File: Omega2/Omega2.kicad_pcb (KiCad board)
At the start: 2 copper layers, 6 parts, among them J1 Conn_01x04_Female, J2 Conn_01x14_Female, SW1 SW_DIP_x01, U1 Omega2+

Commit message: Organización display, botón de reset, power flag
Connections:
- net +3V3 renamed 3.3V
- net Net-(R1-Pad2) renamed Om38
- net Net-(U1-Pad11) renamed Om8
- net Net-(U1-Pad12) renamed Om7
- net Net-(U1-Pad13) renamed Om6
- net Net-(U1-Pad7) renamed Om15
- U1 pad 10: unconnected-(U1-Pad10) -> Om9
- U1 pad 14: unconnected-(U1-Pad14) -> Om1
- U1 pad 15: unconnected-(U1-Pad15) -> Om0
- U1 pad 16: unconnected-(U1-Pad16) -> OmRSTneg
- U1 pad 17: unconnected-(U1-Pad17) -> Om5
- U1 pad 18: unconnected-(U1-Pad18) -> Om4
- U1 pad 19: unconnected-(U1-Pad19) -> Om19
- U1 pad 2: unconnected-(U1-Pad2) -> Om11
- U1 pad 20: unconnected-(U1-Pad20) -> Om18
- U1 pad 21: unconnected-(U1-Pad21) -> OmRx+
- U1 pad 22: unconnected-(U1-Pad22) -> OmRx-
- U1 pad 23: unconnected-(U1-Pad23) -> OmTx+
- U1 pad 24: unconnected-(U1-Pad24) -> OmTx-
- U1 pad 25: unconnected-(U1-Pad25) -> Om3.3V
- U1 pad 27: unconnected-(U1-Pad27) -> Om12
- U1 pad 28: unconnected-(U1-Pad28) -> Om13
- U1 pad 29: unconnected-(U1-Pad29) -> OmUSB-
- U1 pad 3: unconnected-(U1-Pad3) -> Om3
- U1 pad 30: unconnected-(U1-Pad30) -> OmUSB+
- U1 pad 4: unconnected-(U1-Pad4) -> Om2
- U1 pad 5: unconnected-(U1-Pad5) -> Om17
- U1 pad 6: unconnected-(U1-Pad6) -> Om16
- U1 pad 8: unconnected-(U1-Pad8) -> Om46
- U1 pad 9: unconnected-(U1-Pad9) -> Om45

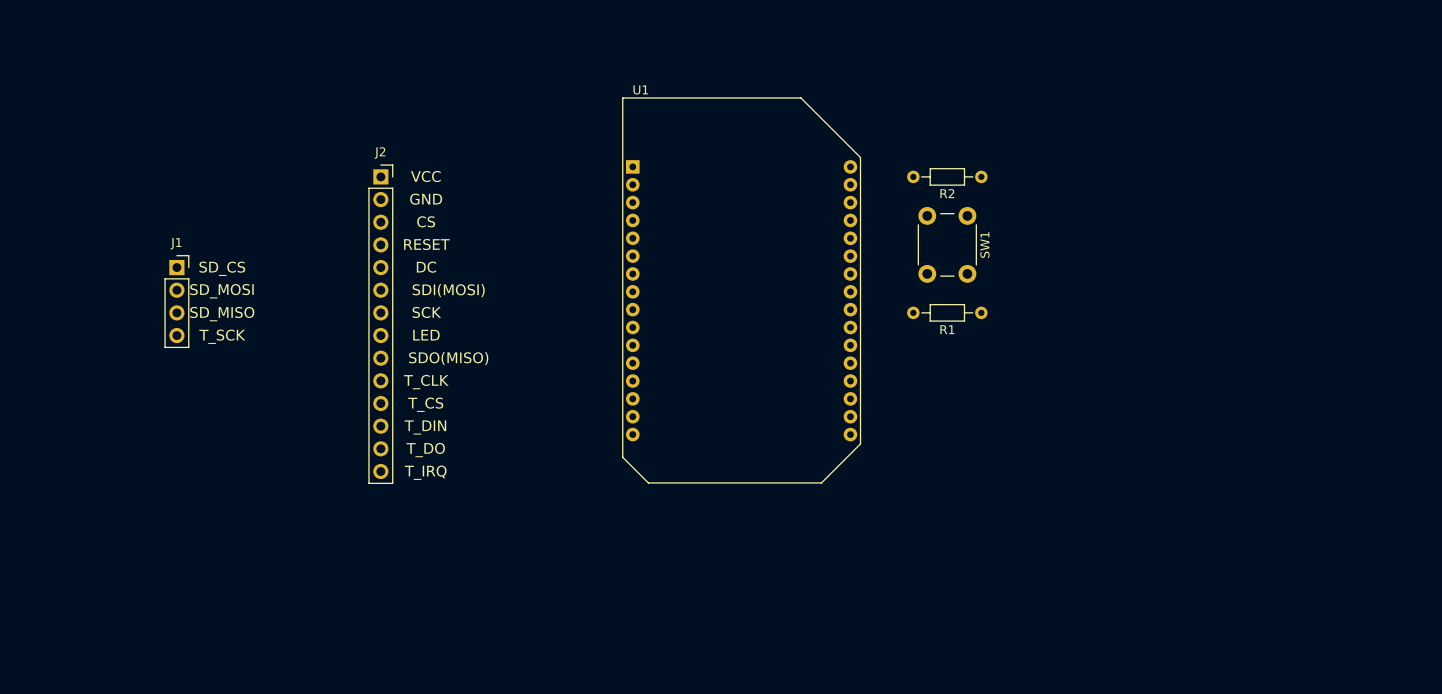
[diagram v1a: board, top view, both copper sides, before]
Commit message: edicion pcb
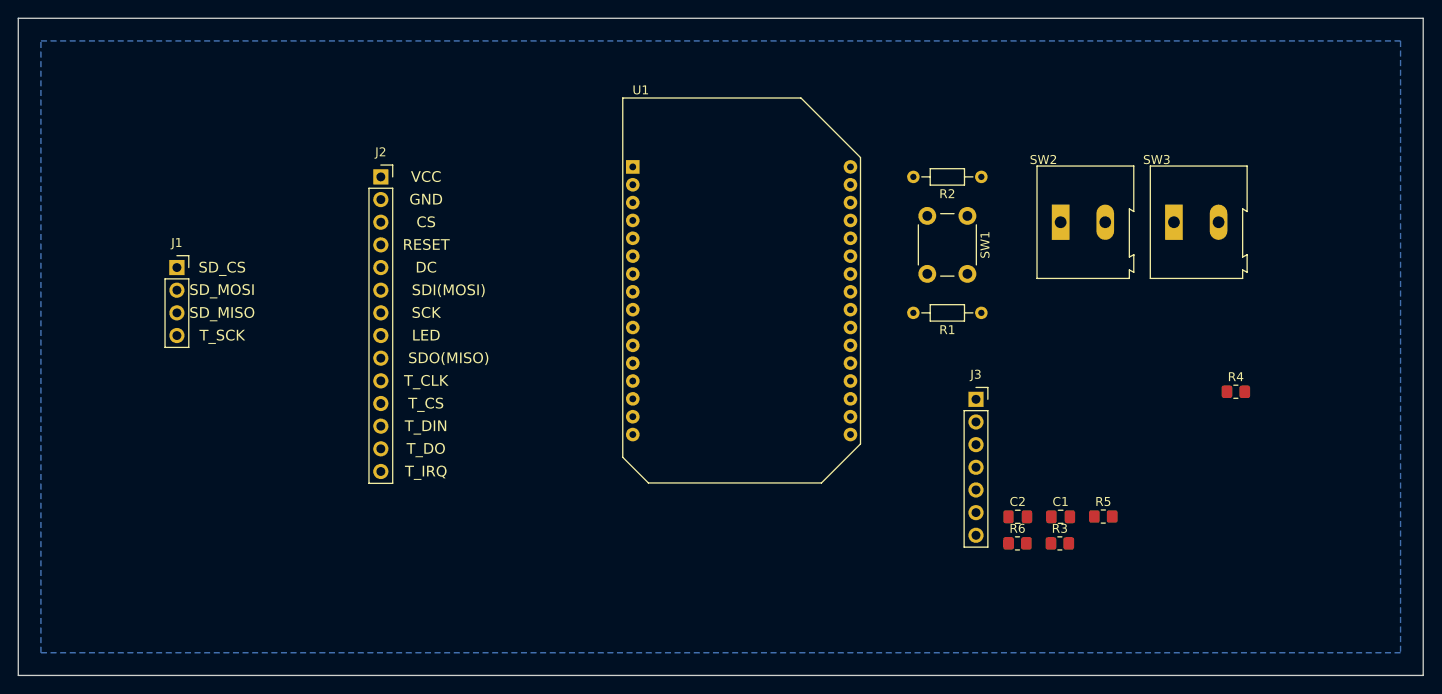
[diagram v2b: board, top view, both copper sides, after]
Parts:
- added C1: 100n, Capacitor_SMD:C_0805_2012Metric_Pad1.18x1.45mm_HandSolder, F.Cu at (170.2, 119.4)
- added C2: 100n, Capacitor_SMD:C_0805_2012Metric_Pad1.18x1.45mm_HandSolder, F.Cu at (165.4, 119.4)
- added J3: Conn_01x07_Female, Connector_PinSocket_2.54mm:PinSocket_1x07_P2.54mm_Vertical, F.Cu at (160.7, 106.2)
- added R3: 51k, Resistor_SMD:R_0805_2012Metric_Pad1.20x1.40mm_HandSolder, F.Cu at (170.1, 122.4)
- added R4: 5.1k, Resistor_SMD:R_0805_2012Metric_Pad1.20x1.40mm_HandSolder, F.Cu at (189.8, 105.4)
- added R5: 51k, Resistor_SMD:R_0805_2012Metric_Pad1.20x1.40mm_HandSolder, F.Cu at (175.0, 119.3)
- added R6: 5.1k, Resistor_SMD:R_0805_2012Metric_Pad1.20x1.40mm_HandSolder, F.Cu at (165.3, 122.4)
- added SW2: FW, TerminalBlock:TerminalBlock_Altech_AK300-2_P5.00mm, F.Cu at (170.2, 86.4)
- added SW3: BW, TerminalBlock:TerminalBlock_Altech_AK300-2_P5.00mm, F.Cu at (182.9, 86.4)
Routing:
- added copper zone on B.Cu, net GND
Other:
- board outline added: 157.5 x 73.7 mm

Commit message: Prueba de ruteo
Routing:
- net 3.3V: track 0.00 -> 179.3 mm
- net Om16: track 0.00 -> 90.1 mm
- net Om17: track 0.00 -> 72.1 mm
- net Om38: track 0.00 -> 71.3 mm
- net Om11: track 0.00 -> 53.5 mm
- net Net-(R6-Pad2): track 0.00 -> 39.1 mm
- net Om13: track 0.00 -> 35.4 mm
- net Om7: track 0.00 -> 33.7 mm
- net Om15: track 0.00 -> 33.2 mm
- net Om6: track 0.00 -> 30.3 mm
- net Om12: track 0.00 -> 29.7 mm
- net Om8: track 0.00 -> 28.8 mm
- net Net-(R4-Pad2): track 0.00 -> 22.3 mm
- net Om19: track 0.00 -> 21.3 mm
- net Om18: track 0.00 -> 20.9 mm
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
